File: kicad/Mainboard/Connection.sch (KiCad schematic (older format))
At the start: 7 parts, among them J12 GPS_CONN, J13 DBG_CONN, J14 KBD_CONN, J15 Micro_SD_Card, U9 ADXL345

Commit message: Updated WIP schematics
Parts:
- removed R29, R30: 4k7, symbol Mainboard-rescue:R_Small-device
- removed U9: ADXL345, symbol TR-9:ADXL345
- added C?: 100n, symbol Device:C_Small
- added C?: 10n, symbol Device:C_Small
- added R? (x2): 4k7, symbol Device:R_Small
- added R? (x4): 10k, symbol Device:R_Small
- added U?: LSM9DS1, Package_LGA:LGA-24L_3x3.5mm_P0.43mm, symbol Sensor_Motion:LSM9DS1
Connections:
- wire segments 49 -> 73
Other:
- note added: "ADDR 0x6B AG, 0x1E M"
- note removed: "ADDR 0x53"
- note removed: "TODO: Maybe add GPS with integrated IMU"

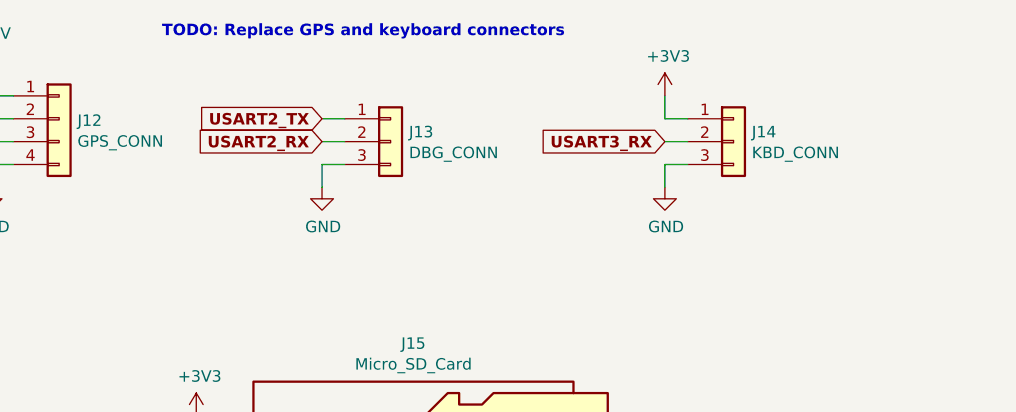
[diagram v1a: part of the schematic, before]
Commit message: Add files via upload
* replaced Q7 with BSS138
* new HMI connector (for keypad and display)
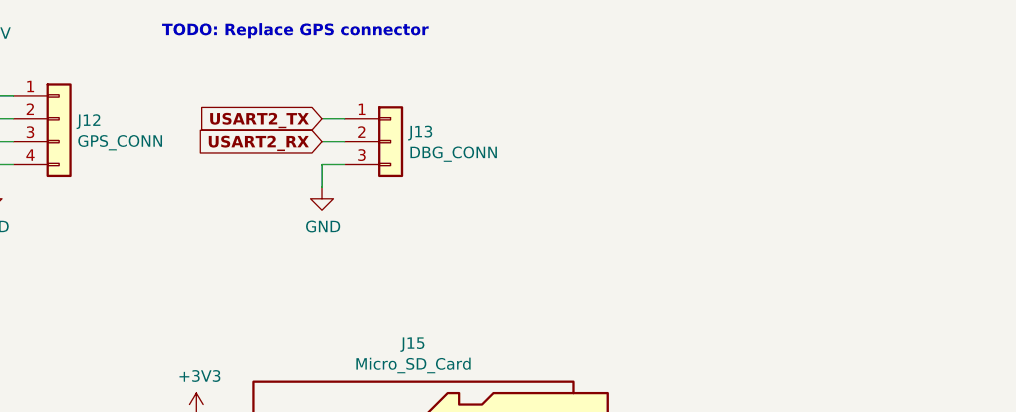
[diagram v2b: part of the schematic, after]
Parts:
- removed J14: KBD_CONN, symbol Mainboard-rescue:Conn_01x03-conn
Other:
- note added: "TODO: Replace GPS connector"
- note removed: "TODO: Replace GPS and keyboard connectors"
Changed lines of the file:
@@
 EESchema Schematic File Version 4
+LIBS:Mainboard-cache
 EELAYER 30 0
 EELAYER END
@@
 	2900 1200 3000 1200
 $Comp
-L Mainboard-rescue:Conn_01x03-conn J14
-U 1 1 5E07E690
-P 4700 1300
-F 0 "J14" H 4780 1342 50  0000 L CNN
-F 1 "KBD_CONN" H 4780 1251 50  0000 L CNN
-F 2 "" H 4700 1300 50  0001 C CNN
-F 3 "~" H 4700 1300 50  0001 C CNN
-	1    4700 1300
-	1    0    0    -1
-$EndComp
-$Comp
-L power:GND #PWR0108
-U 1 1 5E07ED77
-P 4400 1500
-F 0 "#PWR0108" H 4400 1250 50  0001 C CNN
-F 1 "GND" H 4405 1327 50  0000 C CNN
-F 2 "" H 4400 1500 50  0001 C CNN
-F 3 "" H 4400 1500 50  0001 C CNN
-	1    4400 1500
-	1    0    0    -1
-$EndComp
-Wire Wire Line
-	4400 1500 4400 1400
-Wire Wire Line
-	4400 1400 4500 1400
-$Comp
-L power:+3V3 #PWR0105
-U 1 1 5E07F45E
-P 4400 1100
-F 0 "#PWR0105" H 4400 950 50  0001 C CNN
-F 1 "+3V3" H 4415 1273 50  0000 C CNN
-F 2 "" H 4400 1100 50  0001 C CNN
-F 3 "" H 4400 1100 50  0001 C CNN
-	1    4400 1100
-	1    0    0    -1
-$EndComp
-Wire Wire Line
-	4400 1100 4400 1200
-Wire Wire Line
-	4400 1200 4500 1200
-Wire Wire Line
-	4500 1300 4400 1300
-Text GLabel 4400 1300 0    50   Input ~ 10
-USART3_RX
-$Comp
 L Mainboard-rescue:Micro_SD_Card-conn J15
 U 1 1 5E0856B5
@@
 ADDR 0x6B AG, 0x1E M
 Text Notes 2200 850  0    50   ~ 10
-TODO: Replace GPS and keyboard connectors
+TODO: Replace GPS connector
 $Comp
 L Sensor_Motion:LSM9DS1 U?

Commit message: Annotated parts
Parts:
- gave numbers to parts that had none: 9
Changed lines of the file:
@@
 TODO: Replace GPS connector
 $Comp
-L Sensor_Motion:LSM9DS1 U?
+L Sensor_Motion:LSM9DS1 U10
 U 1 1 5E067250
 P 7750 3750
-F 0 "U?" H 7750 3800 50  0000 C CNN
+F 0 "U10" H 7750 3800 50  0000 C CNN
 F 1 "LSM9DS1" H 7750 3700 50  0000 C CNN
 F 2 "Package_LGA:LGA-24L_3x3.5mm_P0.43mm" H 9250 4500 50  0001 C CNN
@@
 $EndComp
 $Comp
-L power:+3V3 #PWR?
+L power:+3V3 #PWR0152
 U 1 1 5E06CB2E
 P 7750 2750
-F 0 "#PWR?" H 7750 2600 50  0001 C CNN
+F 0 "#PWR0152" H 7750 2600 50  0001 C CNN
 F 1 "+3V3" H 7765 2923 50  0000 C CNN
 F 2 "" H 7750 2750 50  0001 C CNN
@@
 Connection ~ 8050 2850
 $Comp
-L power:GND #PWR?
+L power:GND #PWR0151
 U 1 1 5E06F5C7
 P 7650 4750
-F 0 "#PWR?" H 7650 4500 50  0001 C CNN
+F 0 "#PWR0151" H 7650 4500 50  0001 C CNN
 F 1 "GND" H 7655 4577 50  0000 C CNN
 F 2 "" H 7650 4750 50  0001 C CNN
@@
 $EndComp
 $Comp
-L power:GND #PWR?
+L power:GND #PWR0153
 U 1 1 5E06FFF0
 P 7850 4750
-F 0 "#PWR?" H 7850 4500 50  0001 C CNN
+F 0 "#PWR0153" H 7850 4500 50  0001 C CNN
 F 1 "GND" H 7855 4577 50  0000 C CNN
 F 2 "" H 7850 4750 50  0001 C CNN
@@
 $EndComp
 $Comp
-L power:GND #PWR?
+L power:GND #PWR0155
 U 1 1 5E070F61
 P 8550 4750
-F 0 "#PWR?" H 8550 4500 50  0001 C CNN
+F 0 "#PWR0155" H 8550 4500 50  0001 C CNN
 F 1 "GND" H 8555 4577 50  0000 C CNN
 F 2 "" H 8550 4750 50  0001 C CNN
@@
 	8550 3950 8550 4050
 $Comp
-L Device:R_Small R?
+L Device:R_Small R45
 U 1 1 5E07451A
 P 6850 3150
-F 0 "R?" H 6909 3196 50  0000 L CNN
+F 0 "R45" H 6909 3196 50  0000 L CNN
 F 1 "4k7" H 6909 3105 50  0000 L CNN
 F 2 "" H 6850 3150 50  0001 C CNN
@@
 $EndComp
 $Comp
-L Device:R_Small R?
+L Device:R_Small R44
 U 1 1 5E075066
 P 6600 3150
-F 0 "R?" H 6659 3196 50  0000 L CNN
+F 0 "R44" H 6659 3196 50  0000 L CNN
 F 1 "4k7" H 6659 3105 50  0000 L CNN
 F 2 "" H 6600 3150 50  0001 C CNN
@@
 Connection ~ 6850 3450
 $Comp
-L power:+3V3 #PWR?
+L power:+3V3 #PWR0149
 U 1 1 5E0788C1
 P 6850 2950
-F 0 "#PWR?" H 6850 2800 50  0001 C CNN
+F 0 "#PWR0149" H 6850 2800 50  0001 C CNN
 F 1 "+3V3" H 6865 3123 50  0000 C CNN
 F 2 "" H 6850 2950 50  0001 C CNN
@@
 $EndComp
 $Comp
-L power:+3V3 #PWR?
+L power:+3V3 #PWR0148
 U 1 1 5E078F90
 P 6600 2950
-F 0 "#PWR?" H 6600 2800 50  0001 C CNN
+F 0 "#PWR0148" H 6600 2800 50  0001 C CNN
 F 1 "+3V3" H 6615 3123 50  0000 C CNN
 F 2 "" H 6600 2950 50  0001 C CNN
@@
 	6850 2950 6850 3050
 $Comp
-L Device:C_Small C?
+L Device:C_Small C89
 U 1 1 5E07AC5C
 P 6850 4550
-F 0 "C?" H 6942 4596 50  0000 L CNN
+F 0 "C89" H 6942 4596 50  0000 L CNN
 F 1 "100n" H 6942 4505 50  0000 L CNN
 F 2 "" H 6850 4550 50  0001 C CNN
@@
 $EndComp
 $Comp
-L Device:C_Small C?
+L Device:C_Small C88
 U 1 1 5E07BBD5
 P 6500 4550
-F 0 "C?" H 6592 4596 50  0000 L CNN
+F 0 "C88" H 6592 4596 50  0000 L CNN
 F 1 "10n" H 6592 4505 50  0000 L CNN
 F 2 "" H 6500 4550 50  0001 C CNN
@@
 	6850 4350 6850 4450
 $Comp
-L power:GND #PWR?
+L power:GND #PWR0150
 U 1 1 5E07DD63
 P 6850 4750
-F 0 "#PWR?" H 6850 4500 50  0001 C CNN
+F 0 "#PWR0150" H 6850 4500 50  0001 C CNN
 F 1 "GND" H 6855 4577 50  0000 C CNN
 F 2 "" H 6850 4750 50  0001 C CNN
@@
 $EndComp
 $Comp
-L power:GND #PWR?
+L power:GND #PWR0147
 U 1 1 5E07E2EE
 P 6500 4750
-F 0 "#PWR?" H 6500 4500 50  0001 C CNN
+F 0 "#PWR0147" H 6500 4500 50  0001 C CNN
 F 1 "GND" H 6505 4577 50  0000 C CNN
 F 2 "" H 6500 4750 50  0001 C CNN
@@
 	8550 4250 8550 4750
 $Comp
-L Device:R_Small R?
+L Device:R_Small R43
 U 1 1 5E085D7F
 P 6300 3150
-F 0 "R?" H 6359 3196 50  0000 L CNN
+F 0 "R43" H 6359 3196 50  0000 L CNN
 F 1 "10k" H 6359 3105 50  0000 L CNN
 F 2 "" H 6300 3150 50  0001 C CNN
@@
 $EndComp
 $Comp
-L Device:R_Small R?
+L Device:R_Small R46
 U 1 1 5E086057
 P 8550 3150
-F 0 "R?" H 8609 3196 50  0000 L CNN
+F 0 "R46" H 8609 3196 50  0000 L CNN
 F 1 "10k" H 8609 3105 50  0000 L CNN
 F 2 "" H 8550 3150 50  0001 C CNN
@@
 	8550 3350 8550 3250
 $Comp
-L power:+3V3 #PWR?
+L power:+3V3 #PWR0146
 U 1 1 5E089278
 P 6300 2950
-F 0 "#PWR?" H 6300 2800 50  0001 C CNN
+F 0 "#PWR0146" H 6300 2800 50  0001 C CNN
 F 1 "+3V3" H 6315 3123 50  0000 C CNN
 F 2 "" H 6300 2950 50  0001 C CNN
@@
 	6300 2950 6300 3050
 $Comp
-L power:+3V3 #PWR?
+L power:+3V3 #PWR0154
 U 1 1 5E08A7A1
 P 8550 2950
-F 0 "#PWR?" H 8550 2800 50  0001 C CNN
+F 0 "#PWR0154" H 8550 2800 50  0001 C CNN
 F 1 "+3V3" H 8565 3123 50  0000 C CNN
 F 2 "" H 8550 2950 50  0001 C CNN
@@
 NoConn ~ 8450 3550
 $Comp
-L Device:R_Small R?
+L Device:R_Small R47
 U 1 1 5E0918A1
 P 8800 3150
-F 0 "R?" H 8859 3196 50  0000 L CNN
+F 0 "R47" H 8859 3196 50  0000 L CNN
 F 1 "10k" H 8859 3105 50  0000 L CNN
 F 2 "" H 8800 3150 50  0001 C CNN
@@
 	8800 3450 8800 3250
 $Comp
-L Device:R_Small R?
+L Device:R_Small R42
 U 1 1 5E092F27
 P 6050 3150
-F 0 "R?" H 6109 3196 50  0000 L CNN
+F 0 "R42" H 6109 3196 50  0000 L CNN
 F 1 "10k" H 6109 3105 50  0000 L CNN
 F 2 "" H 6050 3150 50  0001 C CNN
@@
 	6050 3750 6050 3250
 $Comp
-L power:+3V3 #PWR?
+L power:+3V3 #PWR0145
 U 1 1 5E09497A
 P 6050 2950
-F 0 "#PWR?" H 6050 2800 50  0001 C CNN
+F 0 "#PWR0145" H 6050 2800 50  0001 C CNN
 F 1 "+3V3" H 6065 3123 50  0000 C CNN
 F 2 "" H 6050 2950 50  0001 C CNN
@@
 	6050 2950 6050 3050
 $Comp
-L power:+3V3 #PWR?
+L power:+3V3 #PWR0156
 U 1 1 5E09620D
 P 8800 2950
-F 0 "#PWR?" H 8800 2800 50  0001 C CNN
+F 0 "#PWR0156" H 8800 2800 50  0001 C CNN
 F 1 "+3V3" H 8815 3123 50  0000 C CNN
 F 2 "" H 8800 2950 50  0001 C CNN

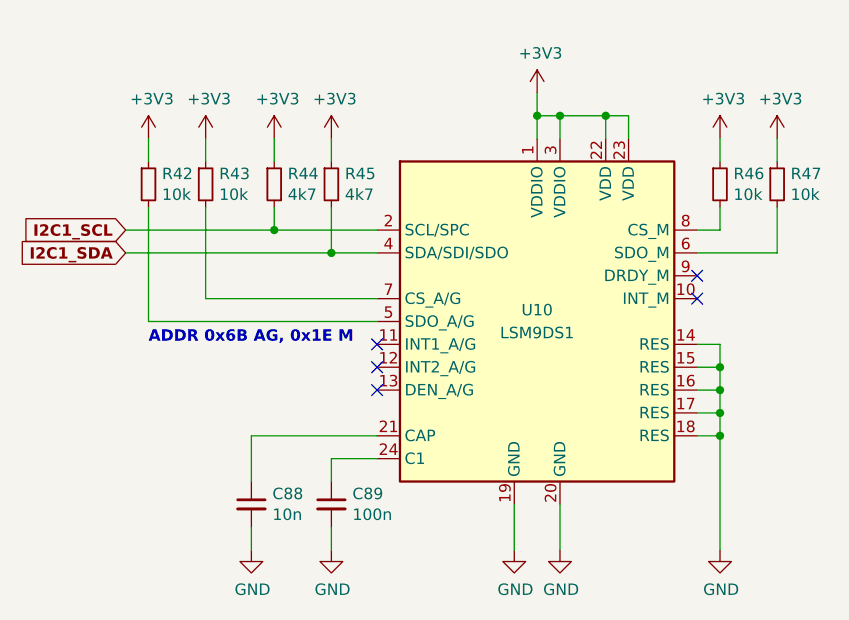
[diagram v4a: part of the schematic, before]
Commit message: Revert "Annotated parts"
This reverts commit b309e3bfe0d7a41f96c10818008ed221b92f9604.
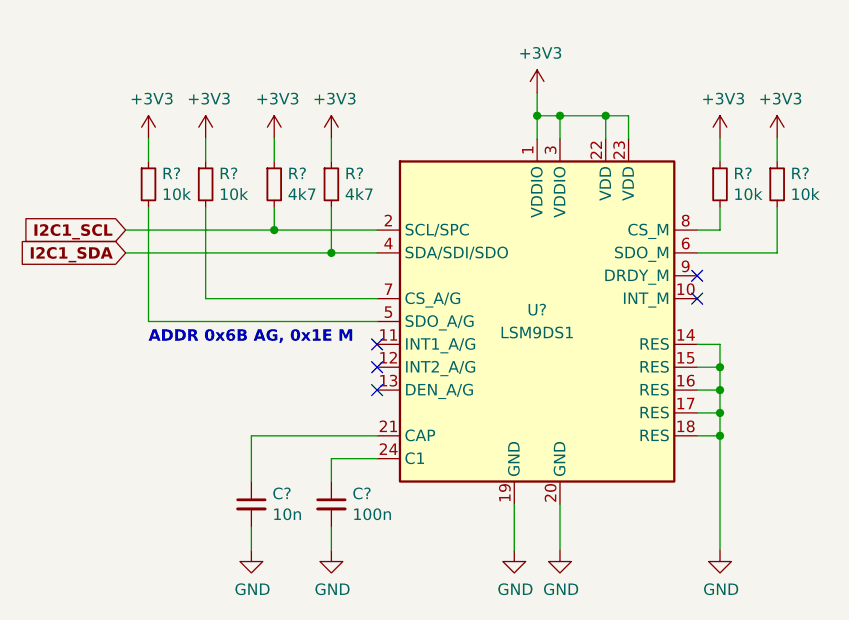
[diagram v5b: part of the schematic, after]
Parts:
- renumbered C89 to C?, C88 to C?, R45 to R?, R44 to R?, R43 to R?, R46 to R?, R47 to R?, R42 to R?, U10 to U?
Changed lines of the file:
@@
 TODO: Replace GPS connector
 $Comp
-L Sensor_Motion:LSM9DS1 U10
+L Sensor_Motion:LSM9DS1 U?
 U 1 1 5E067250
 P 7750 3750
-F 0 "U10" H 7750 3800 50  0000 C CNN
+F 0 "U?" H 7750 3800 50  0000 C CNN
 F 1 "LSM9DS1" H 7750 3700 50  0000 C CNN
 F 2 "Package_LGA:LGA-24L_3x3.5mm_P0.43mm" H 9250 4500 50  0001 C CNN
@@
 $EndComp
 $Comp
-L power:+3V3 #PWR0152
+L power:+3V3 #PWR?
 U 1 1 5E06CB2E
 P 7750 2750
-F 0 "#PWR0152" H 7750 2600 50  0001 C CNN
+F 0 "#PWR?" H 7750 2600 50  0001 C CNN
 F 1 "+3V3" H 7765 2923 50  0000 C CNN
 F 2 "" H 7750 2750 50  0001 C CNN
@@
 Connection ~ 8050 2850
 $Comp
-L power:GND #PWR0151
+L power:GND #PWR?
 U 1 1 5E06F5C7
 P 7650 4750
-F 0 "#PWR0151" H 7650 4500 50  0001 C CNN
+F 0 "#PWR?" H 7650 4500 50  0001 C CNN
 F 1 "GND" H 7655 4577 50  0000 C CNN
 F 2 "" H 7650 4750 50  0001 C CNN
@@
 $EndComp
 $Comp
-L power:GND #PWR0153
+L power:GND #PWR?
 U 1 1 5E06FFF0
 P 7850 4750
-F 0 "#PWR0153" H 7850 4500 50  0001 C CNN
+F 0 "#PWR?" H 7850 4500 50  0001 C CNN
 F 1 "GND" H 7855 4577 50  0000 C CNN
 F 2 "" H 7850 4750 50  0001 C CNN
@@
 $EndComp
 $Comp
-L power:GND #PWR0155
+L power:GND #PWR?
 U 1 1 5E070F61
 P 8550 4750
-F 0 "#PWR0155" H 8550 4500 50  0001 C CNN
+F 0 "#PWR?" H 8550 4500 50  0001 C CNN
 F 1 "GND" H 8555 4577 50  0000 C CNN
 F 2 "" H 8550 4750 50  0001 C CNN
@@
 	8550 3950 8550 4050
 $Comp
-L Device:R_Small R45
+L Device:R_Small R?
 U 1 1 5E07451A
 P 6850 3150
-F 0 "R45" H 6909 3196 50  0000 L CNN
+F 0 "R?" H 6909 3196 50  0000 L CNN
 F 1 "4k7" H 6909 3105 50  0000 L CNN
 F 2 "" H 6850 3150 50  0001 C CNN
@@
 $EndComp
 $Comp
-L Device:R_Small R44
+L Device:R_Small R?
 U 1 1 5E075066
 P 6600 3150
-F 0 "R44" H 6659 3196 50  0000 L CNN
+F 0 "R?" H 6659 3196 50  0000 L CNN
 F 1 "4k7" H 6659 3105 50  0000 L CNN
 F 2 "" H 6600 3150 50  0001 C CNN
@@
 Connection ~ 6850 3450
 $Comp
-L power:+3V3 #PWR0149
+L power:+3V3 #PWR?
 U 1 1 5E0788C1
 P 6850 2950
-F 0 "#PWR0149" H 6850 2800 50  0001 C CNN
+F 0 "#PWR?" H 6850 2800 50  0001 C CNN
 F 1 "+3V3" H 6865 3123 50  0000 C CNN
 F 2 "" H 6850 2950 50  0001 C CNN
@@
 $EndComp
 $Comp
-L power:+3V3 #PWR0148
+L power:+3V3 #PWR?
 U 1 1 5E078F90
 P 6600 2950
-F 0 "#PWR0148" H 6600 2800 50  0001 C CNN
+F 0 "#PWR?" H 6600 2800 50  0001 C CNN
 F 1 "+3V3" H 6615 3123 50  0000 C CNN
 F 2 "" H 6600 2950 50  0001 C CNN
@@
 	6850 2950 6850 3050
 $Comp
-L Device:C_Small C89
+L Device:C_Small C?
 U 1 1 5E07AC5C
 P 6850 4550
-F 0 "C89" H 6942 4596 50  0000 L CNN
+F 0 "C?" H 6942 4596 50  0000 L CNN
 F 1 "100n" H 6942 4505 50  0000 L CNN
 F 2 "" H 6850 4550 50  0001 C CNN
@@
 $EndComp
 $Comp
-L Device:C_Small C88
+L Device:C_Small C?
 U 1 1 5E07BBD5
 P 6500 4550
-F 0 "C88" H 6592 4596 50  0000 L CNN
+F 0 "C?" H 6592 4596 50  0000 L CNN
 F 1 "10n" H 6592 4505 50  0000 L CNN
 F 2 "" H 6500 4550 50  0001 C CNN
@@
 	6850 4350 6850 4450
 $Comp
-L power:GND #PWR0150
+L power:GND #PWR?
 U 1 1 5E07DD63
 P 6850 4750
-F 0 "#PWR0150" H 6850 4500 50  0001 C CNN
+F 0 "#PWR?" H 6850 4500 50  0001 C CNN
 F 1 "GND" H 6855 4577 50  0000 C CNN
 F 2 "" H 6850 4750 50  0001 C CNN
@@
 $EndComp
 $Comp
-L power:GND #PWR0147
+L power:GND #PWR?
 U 1 1 5E07E2EE
 P 6500 4750
-F 0 "#PWR0147" H 6500 4500 50  0001 C CNN
+F 0 "#PWR?" H 6500 4500 50  0001 C CNN
 F 1 "GND" H 6505 4577 50  0000 C CNN
 F 2 "" H 6500 4750 50  0001 C CNN
@@
 	8550 4250 8550 4750
 $Comp
-L Device:R_Small R43
+L Device:R_Small R?
 U 1 1 5E085D7F
 P 6300 3150
-F 0 "R43" H 6359 3196 50  0000 L CNN
+F 0 "R?" H 6359 3196 50  0000 L CNN
 F 1 "10k" H 6359 3105 50  0000 L CNN
 F 2 "" H 6300 3150 50  0001 C CNN
@@
 $EndComp
 $Comp
-L Device:R_Small R46
+L Device:R_Small R?
 U 1 1 5E086057
 P 8550 3150
-F 0 "R46" H 8609 3196 50  0000 L CNN
+F 0 "R?" H 8609 3196 50  0000 L CNN
 F 1 "10k" H 8609 3105 50  0000 L CNN
 F 2 "" H 8550 3150 50  0001 C CNN
@@
 	8550 3350 8550 3250
 $Comp
-L power:+3V3 #PWR0146
+L power:+3V3 #PWR?
 U 1 1 5E089278
 P 6300 2950
-F 0 "#PWR0146" H 6300 2800 50  0001 C CNN
+F 0 "#PWR?" H 6300 2800 50  0001 C CNN
 F 1 "+3V3" H 6315 3123 50  0000 C CNN
 F 2 "" H 6300 2950 50  0001 C CNN
@@
 	6300 2950 6300 3050
 $Comp
-L power:+3V3 #PWR0154
+L power:+3V3 #PWR?
 U 1 1 5E08A7A1
 P 8550 2950
-F 0 "#PWR0154" H 8550 2800 50  0001 C CNN
+F 0 "#PWR?" H 8550 2800 50  0001 C CNN
 F 1 "+3V3" H 8565 3123 50  0000 C CNN
 F 2 "" H 8550 2950 50  0001 C CNN
@@
 NoConn ~ 8450 3550
 $Comp
-L Device:R_Small R47
+L Device:R_Small R?
 U 1 1 5E0918A1
 P 8800 3150
-F 0 "R47" H 8859 3196 50  0000 L CNN
+F 0 "R?" H 8859 3196 50  0000 L CNN
 F 1 "10k" H 8859 3105 50  0000 L CNN
 F 2 "" H 8800 3150 50  0001 C CNN
@@
 	8800 3450 8800 3250
 $Comp
-L Device:R_Small R42
+L Device:R_Small R?
 U 1 1 5E092F27
 P 6050 3150
-F 0 "R42" H 6109 3196 50  0000 L CNN
+F 0 "R?" H 6109 3196 50  0000 L CNN
 F 1 "10k" H 6109 3105 50  0000 L CNN
 F 2 "" H 6050 3150 50  0001 C CNN
@@
 	6050 3750 6050 3250
 $Comp
-L power:+3V3 #PWR0145
+L power:+3V3 #PWR?
 U 1 1 5E09497A
 P 6050 2950
-F 0 "#PWR0145" H 6050 2800 50  0001 C CNN
+F 0 "#PWR?" H 6050 2800 50  0001 C CNN
 F 1 "+3V3" H 6065 3123 50  0000 C CNN
 F 2 "" H 6050 2950 50  0001 C CNN
@@
 	6050 2950 6050 3050
 $Comp
-L power:+3V3 #PWR0156
+L power:+3V3 #PWR?
 U 1 1 5E09620D
 P 8800 2950
-F 0 "#PWR0156" H 8800 2800 50  0001 C CNN
+F 0 "#PWR?" H 8800 2800 50  0001 C CNN
 F 1 "+3V3" H 8815 3123 50  0000 C CNN
 F 2 "" H 8800 2950 50  0001 C CNN

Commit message: Add files via upload
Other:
- moved on the sheet: C?, J12, J13, J15, R?, U?

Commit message: Add files via upload
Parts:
- removed J12: GPS_CONN, symbol Mainboard-rescue:Conn_01x04-conn
- added J?: GPS_CONN, symbol Connector_Generic:Conn_01x05
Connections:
- net +5V: now also J?.1 (Pin_1)
- net GND: now also J?.5 (Pin_5)
- net USART1_RX: now also J?.3 (Pin_3)
- net USART1_TX: now also J?.2 (Pin_2)
- new net GPS_EN: J?.4 (Pin_4)
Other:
- note removed: "TODO: Replace GPS connector"
- moved on the sheet: J13
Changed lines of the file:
@@
 $Descr A4 11693 8268
 encoding utf-8
-Sheet 7 7
+Sheet 7 8
 Title "Connections"
 Date ""
@@
 $EndDescr
 $Comp
-L Mainboard-rescue:Conn_01x04-conn J12
-U 1 1 5E07BAA3
-P 3300 1950
-F 0 "J12" H 3380 1942 50  0000 L CNN
-F 1 "GPS_CONN" H 3380 1851 50  0000 L CNN
-F 2 "" H 3300 1950 50  0001 C CNN
-F 3 "~" H 3300 1950 50  0001 C CNN
-	1    3300 1950
-	1    0    0    -1
-$EndComp
-$Comp
 L power:+5V #PWR0104
 U 1 1 5E07BDC5
@@
 L power:GND #PWR0106
 U 1 1 5E07C3FA
-P 3000 2250
-F 0 "#PWR0106" H 3000 2000 50  0001 C CNN
-F 1 "GND" H 3005 2077 50  0000 C CNN
-F 2 "" H 3000 2250 50  0001 C CNN
-F 3 "" H 3000 2250 50  0001 C CNN
-	1    3000 2250
-	1    0    0    -1
-$EndComp
-Wire Wire Line
-	3000 2250 3000 2150
-Wire Wire Line
-	3000 2150 3100 2150
+P 3000 2350
+F 0 "#PWR0106" H 3000 2100 50  0001 C CNN
+F 1 "GND" H 3005 2177 50  0000 C CNN
+F 2 "" H 3000 2350 50  0001 C CNN
+F 3 "" H 3000 2350 50  0001 C CNN
+	1    3000 2350
+	1    0    0    -1
+$EndComp
+Wire Wire Line
+	3000 2350 3000 2250
+Wire Wire Line
+	3000 2250 3100 2250
 Wire Wire Line
 	3100 1950 3000 1950
@@
 L Mainboard-rescue:Conn_01x03-conn J13
 U 1 1 5E07CB74
-P 4750 2050
-F 0 "J13" H 4830 2092 50  0000 L CNN
-F 1 "DBG_CONN" H 4830 2001 50  0000 L CNN
-F 2 "" H 4750 2050 50  0001 C CNN
-F 3 "~" H 4750 2050 50  0001 C CNN
-	1    4750 2050
-	1    0    0    -1
-$EndComp
-Text GLabel 4450 1950 0    50   Input ~ 10
+P 4800 2150
+F 0 "J13" H 4880 2192 50  0000 L CNN
+F 1 "DBG_CONN" H 4880 2101 50  0000 L CNN
+F 2 "" H 4800 2150 50  0001 C CNN
+F 3 "~" H 4800 2150 50  0001 C CNN
+	1    4800 2150
+	1    0    0    -1
+$EndComp
+Text GLabel 4500 2050 0    50   Input ~ 10
 USART2_TX
-Text GLabel 4450 2050 0    50   Input ~ 10
+Text GLabel 4500 2150 0    50   Input ~ 10
 USART2_RX
 $Comp
 L power:GND #PWR0107
 U 1 1 5E07D3F6
-P 4450 2250
-F 0 "#PWR0107" H 4450 2000 50  0001 C CNN
-F 1 "GND" H 4455 2077 50  0000 C CNN
-F 2 "" H 4450 2250 50  0001 C CNN
-F 3 "" H 4450 2250 50  0001 C CNN
-	1    4450 2250
-	1    0    0    -1
-$EndComp
-Wire Wire Line
-	4450 2250 4450 2150
-Wire Wire Line
-	4450 2150 4550 2150
-Wire Wire Line
-	4450 2050 4550 2050
-Wire Wire Line
-	4450 1950 4550 1950
+P 4500 2350
+F 0 "#PWR0107" H 4500 2100 50  0001 C CNN
+F 1 "GND" H 4505 2177 50  0000 C CNN
+F 2 "" H 4500 2350 50  0001 C CNN
+F 3 "" H 4500 2350 50  0001 C CNN
+	1    4500 2350
+	1    0    0    -1
+$EndComp
+Wire Wire Line
+	4500 2350 4500 2250
+Wire Wire Line
+	4500 2250 4600 2250
+Wire Wire Line
+	4500 2150 4600 2150
+Wire Wire Line
+	4500 2050 4600 2050
 $Comp
 L Mainboard-rescue:Micro_SD_Card-conn J15
@@
 Text Notes 6700 3950 0    50   ~ 10
 ADDR 0x6B AG, 0x1E M
-Text Notes 3750 1600 0    50   ~ 10
-TODO: Replace GPS connector
 $Comp
 L Sensor_Motion:LSM9DS1 U?
@@
 Wire Wire Line
 	6600 3550 7500 3550
+$Comp
+L Connector_Generic:Conn_01x05 J?
+U 1 1 5E3E7A55
+P 3300 2050
+F 0 "J?" H 3380 2092 50  0000 L CNN
+F 1 "GPS_CONN" H 3380 2001 50  0000 L CNN
+F 2 "" H 3300 2050 50  0001 C CNN
+F 3 "~" H 3300 2050 50  0001 C CNN
+	1    3300 2050
+	1    0    0    -1
+$EndComp
+Wire Wire Line
+	3000 2150 3100 2150
+Text GLabel 3000 2150 0    50   Input ~ 10
+GPS_EN
 $EndSCHEMATC
